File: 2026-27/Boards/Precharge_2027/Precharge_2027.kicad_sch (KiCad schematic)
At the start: 88 parts, among them J1 0430450812, J2 Conn_01x04_Pin, J3 Conn_01x02_Pin, Q1 XR6005, Q2 XR6005, Q3 AO3407, Q5 AO3407, U1 H11L1, U2 LM331N, U4 H11L1, U5 LM331N, U7 STM32C011F6P6, U8 UA78M33QDCYRQ1, X1 X50328MSB2GI

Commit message: Update Precharge 2027
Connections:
- net at Molex1.1 (Pin_1): now also F2.2, Molex1.2 (Pin_2)
- net at Molex3.1 (Pin_1): now also F3.2, Molex3.2 (Pin_2)
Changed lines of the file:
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@@
+	)
+	(junction
+		(at 22.86 52.07)
+		(diameter 0)
+		(color 0 0 0 0)
 	)
 	(junction
@@
 	)
 	(junction
+		(at 22.86 181.61)
+		(diameter 0)
+		(color 0 0 0 0)
+	)
+	(junction
 		(at 173.99 41.91)
 		(diameter 0)
@@
 	)
 	(junction
-		(at 22.86 181.61)
-		(diameter 0)
-		(color 0 0 0 0)
-	)
-	(junction
 		(at 266.7 124.46)
 		(diameter 0)
@@
 	)
 	(junction
+		(at 22.86 108.585)
+		(diameter 0)
+		(color 0 0 0 0)
+	)
+	(junction
 		(at 135.255 65.405)
 		(diameter 0)
@@
 	)
 	(junction
+		(at 22.86 128.27)
+		(diameter 0)
+		(color 0 0 0 0)
+	)
+	(junction
 		(at 300.99 114.3)
 		(diameter 0)
@@
 	(junction
 		(at 115.57 68.58)
-		(diameter 0)
-		(color 0 0 0 0)
-	)
-	(junction
-		(at 22.86 107.95)
 		(diameter 0)
 		(color 0 0 0 0)
@@
 	(wire
 		(pts
-			(xy 22.86 107.95) (xy 22.86 110.49)
+			(xy 22.86 107.95) (xy 22.86 108.585)
 		)
 		(stroke
@@
 	(wire
 		(pts
+			(xy 22.86 108.585) (xy 50.165 108.585)
+		)
+		(stroke
+			(width 0)
+			(type default)
+		)
+	)
+	(wire
+		(pts
 			(xy 307.975 73.025) (xy 307.975 77.47)
 		)
@@
 	(wire
 		(pts
-			(xy 22.86 107.95) (xy 50.8 107.95)
-		)
-		(stroke
-			(width 0)
-			(type default)
-		)
-	)
-	(wire
-		(pts
 			(xy 132.08 109.22) (xy 132.08 113.03)
 		)
@@
 	(wire
 		(pts
+			(xy 22.86 52.07) (xy 22.86 54.61)
+		)
+		(stroke
+			(width 0)
+			(type default)
+		)
+	)
+	(wire
+		(pts
 			(xy 335.28 181.61) (xy 339.09 181.61)
 		)
@@
 	(wire
 		(pts
+			(xy 50.165 108.585) (xy 50.8 107.95)
+		)
+		(stroke
+			(width 0)
+			(type default)
+		)
+	)
+	(wire
+		(pts
 			(xy 71.12 146.05) (xy 80.01 146.05)
 		)
@@
 	(wire
 		(pts
+			(xy 22.86 108.585) (xy 22.86 110.49)
+		)
+		(stroke
+			(width 0)
+			(type default)
+		)
+	)
+	(wire
+		(pts
 			(xy 133.35 186.69) (xy 134.62 186.69)
 		)
@@
 	(wire
 		(pts
+			(xy 76.2 96.52) (xy 78.74 96.52)
+		)
+		(stroke
+			(width 0)
+			(type default)
+		)
+	)
+	(wire
+		(pts
+			(xy 170.18 154.94) (xy 161.29 154.94)
+		)
+		(stroke
+			(width 0)
+			(type default)
+		)
+	)
+	(wire
+		(pts
+			(xy 22.86 128.27) (xy 22.86 130.81)
+		)
+		(stroke
+			(width 0)
+			(type default)
+		)
+	)
+	(wire
+		(pts
+			(xy 220.98 29.21) (xy 218.44 29.21)
+		)
+		(stroke
+			(width 0)
+			(type default)
+		)
+	)
+	(wire
+		(pts
+			(xy 310.515 73.025) (xy 310.515 77.47)
+		)
+		(stroke
+			(width 0)
+			(type default)
+		)
+	)
+	(wire
+		(pts
+			(xy 50.8 93.98) (xy 54.61 93.98)
+		)
+		(stroke
+			(width 0)
+			(type default)
+		)
+	)
+	(wire
+		(pts
 			(xy 22.86 181.61) (xy 46.99 181.61)
 		)
 		(stroke
-			(width 0)
-			(type default)
-		)
-	)
-	(wire
-		(pts
-			(xy 76.2 96.52) (xy 78.74 96.52)
-		)
-		(stroke
-			(width 0)
-			(type default)
-		)
-	)
-	(wire
-		(pts
-			(xy 170.18 154.94) (xy 161.29 154.94)
-		)
-		(stroke
-			(width 0)
-			(type default)
-		)
-	)
-	(wire
-		(pts
-			(xy 220.98 29.21) (xy 218.44 29.21)
-		)
-		(stroke
-			(width 0)
-			(type default)
-		)
-	)
-	(wire
-		(pts
-			(xy 310.515 73.025) (xy 310.515 77.47)
-		)
-		(stroke
-			(width 0)
-			(type default)
-		)
-	)
-	(wire
-		(pts
-			(xy 50.8 93.98) (xy 54.61 93.98)
-		)
-		(stroke

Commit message: Precharge 2027 Changes, outlined in Discord, Systems-Electric
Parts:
- removed C1: 22uF, easyeda2kicad:C0805, symbol easyeda2kicad:CL21A226MAQNNNE
- removed D3: PESD15VS1UB, Diode_SMD:D_SOD-523, symbol Diode:PESD3V3S1UL
- removed PS1: TBA_1-1212E, footprints:CONV_TBA_1-1212E, symbol TBA_1-1212E:TBA_1-1212E
- removed TP1, TP2: TestPoint, TestPoint:TestPoint_Pad_D3.0mm, symbol Connector:TestPoint
- removed U8: UA78M33QDCYRQ1, easyeda2kicad:SOT-223-3_L6.5-W3.4-P2.30-LS7.0-BR, symbol easyeda2kicad:UA78M33QDCYRG4Q1
- added C1: C2012X5R1V226MT000E, easyeda2kicad:C0805, symbol easyeda2kicad:C2012X5R1V226MT000E
- added D1: SMAJ30CA_C10755, easyeda2kicad:SMA_L4.4-W2.6-LS5.0-BI, symbol easyeda2kicad:SMAJ30CA_C10755
- added PS1: IM2412SA, IM2405S, symbol easyeda2kicad:IM2412SA
- added U3: MIC5239-3.3YS, easyeda2kicad:SOT-223-3_L6.7-W3.7-P2.30-LS7.0-BR, symbol easyeda2kicad:MIC5239-3.3YS
- D4, D5: value MMBZ16VALT1G -> MMBZ33VALT1G; symbol easyeda2kicad:MMBZ16VALT1G -> easyeda2kicad:MMBZ33VALT1G; LCSC Part C891696 -> C185935; MPN MMBZ16VALT1G -> MMBZ33VALT1G
- Q3, Q5: value AO3407 -> DMP510DL-7; symbol easyeda2kicad:AO3407 -> easyeda2kicad:DMP510DL-7; LCSC Part C181093 -> C397953; MPN AO3407 -> DMP510DL-7; Manufacturer Hottech(合科泰) -> DIODES(美台)
- R18, R30: footprint easyeda2kicad:R0603 -> easyeda2kicad:R0805; symbol easyeda2kicad:0603WAJ0103T5E -> easyeda2kicad:0805W8F1002T5E; LCSC Part C15401 -> C17414; MPN (none) -> 0805W8F1002T5E; Manufacturer (none) -> UNI-ROYAL(厚声)
- R19, R29: footprint easyeda2kicad:R0603 -> easyeda2kicad:R0805; symbol easyeda2kicad:0603WAF3302T5E -> easyeda2kicad:0805W8F3302T5E; LCSC Part C4216 -> C17633; MPN (none) -> 0805W8F3302T5E; Manufacturer (none) -> UNI-ROYAL(厚声)
- ZD6: renamed from D6; value BZT52C10S -> BZT52C24_C2109; footprint Diode_SMD:D_SOD-323 -> easyeda2kicad:SOD-123_L2.8-W1.8-LS3.7-RD; symbol PCM_JLCPCB-Diodes:Zener,BZT52C10S -> easyeda2kicad:BZT52C24_C2109; Attrition Qty 6 -> (none); Category Diodes,Zener Diodes -> (none); Class Preferred Component -> (none); LCSC C19077446 -> (none); LCSC Part (none) -> C2109; MPN (none) -> BZT52C24; Manufacturer hongjiacheng -> CJ(江苏长电/长晶); Minimum Qty 20 -> (none); Part BZT52C10S -> (none); Price 0.019USD -> (none); Process SMT -> (none); Stock 178615 -> (none)
- renumbered F3 to F1
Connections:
- net 12V_HV: now also D1.2 (A), PS1.6 (+V_OUTPUT)
- net 3.3 V: now also C14.2, U3.3 (OUT); no longer C14.1
- net GLV+: now also C1.2, PS1.2 (+V_INPUT), U3.1 (IN)
- net GLV-: now also C14.1, C1.1, PS1.1 (-V_INPUT), PS1.3 (REMOTE_ON/OFF), U3.2 (GND), U3.4 (GND); no longer C14.2
- net HV-: now also D1.1 (K), PS1.9 (-V_OUTPUT)
- no-connect marks 6 -> 8
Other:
- note added: "3.3V LDO Source"
- note added: "33V ESD/Surge TVS Zener Diodes"
- note added: "Active Low Signals"
- note added: "Charge Mode"
- note added: "Charge_on is tied to GND in the charge cart, and floating (pulled high)when not connected to the charge cart so CHG is ON or OFF respectively"
- note added: "Isolated 12V source"
- note added: "MCU"
- note added: "Post AIR Voltage to Frequency Converter"
- note added: "Pre AIR Voltage to Frequency Converter"
- note removed: "Charge_on is tied to GND in the charge cart, and floating (pulled high) when not connected to the charge cart so CHG is ON or OFF respectively"
- note removed: "Isolated 12V source LV side HV side"
- note removed: "active low signals"
- moved on the sheet: C10, C11, C14, C15, C16, C17, C2, C3, C4, C5, C6, C7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

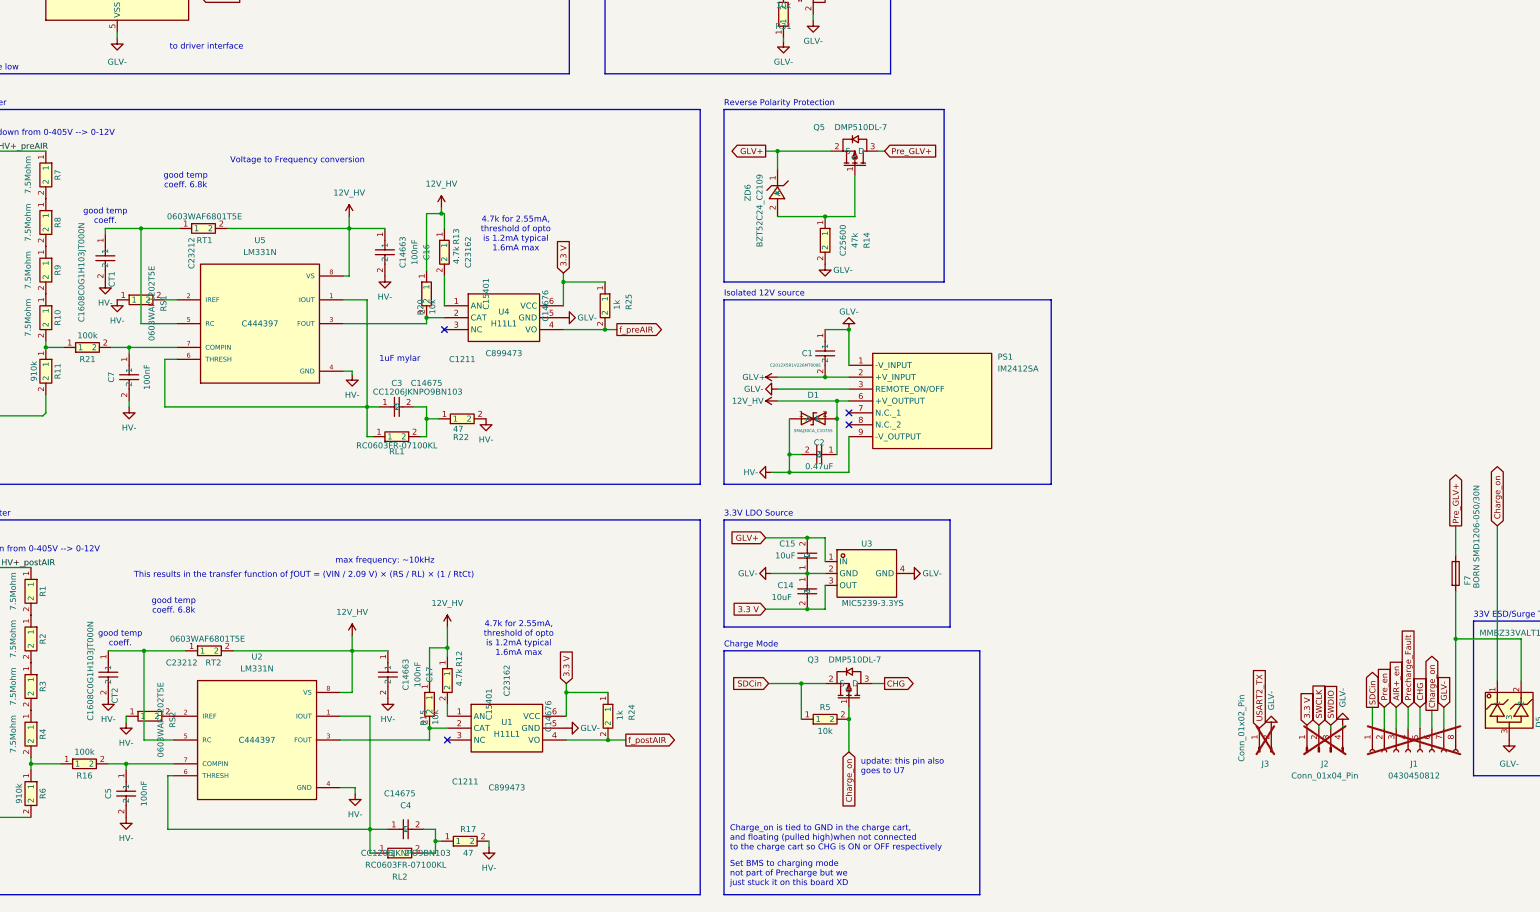
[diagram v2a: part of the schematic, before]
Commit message: precharge 2027 isolation fixing, passing it to Nick for layout
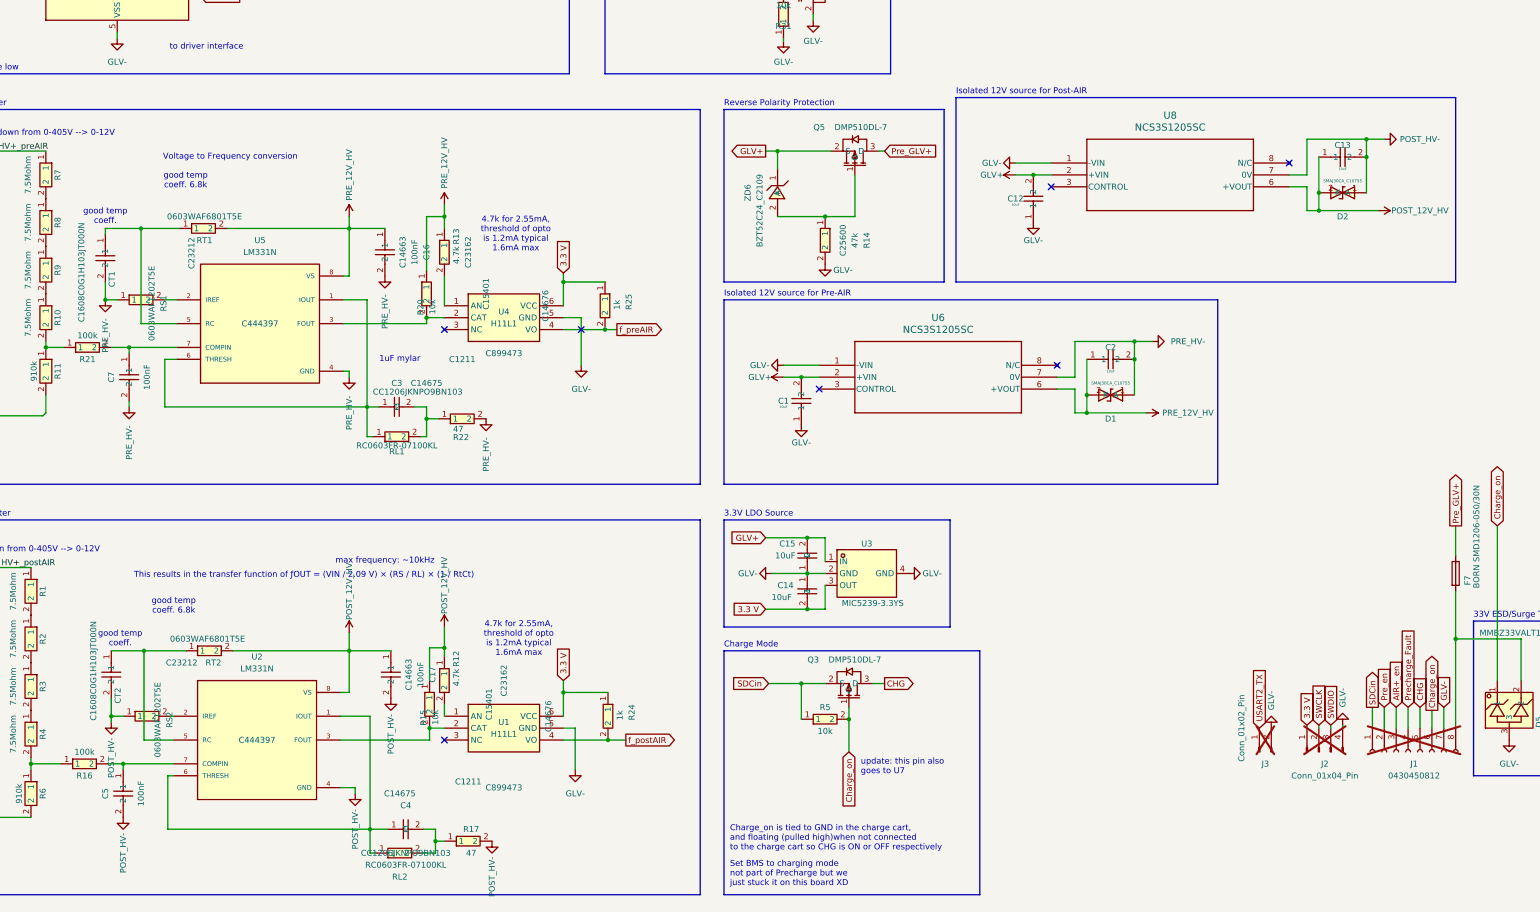
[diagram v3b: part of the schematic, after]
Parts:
- removed PS1: IM2412SA, IM2405S, symbol easyeda2kicad:IM2412SA
- added C12, C13: 10uF, easyeda2kicad:C0805, symbol easyeda2kicad:GRM21BR61H106KE43L
- added D2: SMAJ30CA_C10755, easyeda2kicad:SMA_L4.4-W2.6-LS5.0-BI, symbol easyeda2kicad:SMAJ30CA_C10755
- added U6, U8: NCS3S1205SC, easyeda2kicad:NCS3S1205SC_MUR, symbol easyeda2kicad:NCS3S1205SC
- C1: value C2012X5R1V226MT000E -> 10uF; symbol easyeda2kicad:C2012X5R1V226MT000E -> easyeda2kicad:GRM21BR61H106KE43L; LCSC Part C338080 -> C440198; MPN C2012X5R1V226MT000E -> GRM21BR61H106KE43L; Manufacturer TDK -> muRata(村田)
- C2: value 0.47uF -> 10uF; symbol easyeda2kicad:CL21B474KBFNNNE -> easyeda2kicad:GRM21BR61H106KE43L; LCSC Part C13967 -> C440198; MPN (none) -> GRM21BR61H106KE43L; Manufacturer (none) -> muRata(村田)
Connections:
- net GLV+: now also C12.2, U6.2 (+VIN), U8.2 (+VIN)
- net GLV-: now also C12.1, U6.1 (-VIN), U8.1 (-VIN)
- net 12V_HV renamed PRE_12V_HV
- net PRE_12V_HV: now also U6.6 (+VOUT); no longer C17.1, R12.1, R15.1, RT2.2, U2.8 (VS)
- net HV- renamed PRE_HV-
- net PRE_HV-: now also U6.7 (0V); no longer C17.2, C5.2, CT2.2, R17.2, RS2.1, U2.4 (GND)
- new net POST_12V_HV: C13.1, C17.1, D2.2 (A), R12.1, R15.1, RT2.2, U2.8 (VS), U8.6 (+VOUT)
- new net POST_HV-: C13.2, C17.2, C5.2, CT2.2, D2.1 (K), R17.2, RS2.1, U2.4 (GND), U8.7 (0V)
- no-connect marks 8 -> 11
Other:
- note added: "Isolated 12V source for Post-AIR"
- note added: "Isolated 12V source for Pre-AIR"
- note removed: "Isolated 12V source"
- moved on the sheet: C1, C17, C2, C5, CT2, D1, R12, R17, RS2, U1

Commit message: Update Precharge 2027 design
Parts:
- C3, C4: value CC1206JKNPO9BN103 -> 100nF C0G; symbol easyeda2kicad:CC1206JKNPO9BN103 -> easyeda2kicad:CC1206JKNPO9BN104; LCSC Part C326648 -> C577121; MPN CC1206JKNPO9BN103 -> CC1206JKNPO9BN104; Manufacturer YAGEO(国巨) -> YAGEO
- R1, R10, R2, R3, R4, R7, R8, R9: value 7.5Mohm -> 1.00M; symbol easyeda2kicad:FRC1206F7504TS -> easyeda2kicad:RT1206BRD071ML; LCSC Part C2999556 -> C309662; MPN FRC1206F7504TS -> RT1206BRD071ML; Manufacturer FOJAN(富捷) -> YAGEO
- R11, R6: value 910k -> 80.6k; symbol easyeda2kicad:FRC0603F9103TS -> easyeda2kicad:RT0603BRD0780K6L; LCSC Part C2907075 -> C861568; MPN FRC0603F9103TS -> RT0603BRD0780K6L; Manufacturer FOJAN(富捷) -> YAGEO
- R16, R21: value 100k -> 21.0k; symbol easyeda2kicad:0603WAJ0104T5E -> easyeda2kicad:RT0603BRD0721KL; LCSC Part C15458 -> C861228; MPN (none) -> RT0603BRD0721KL; Manufacturer (none) -> YAGEO
- RL1, RL2: value RC0603FR-07100KL -> 100k; symbol easyeda2kicad:RC0603FR-07100KL -> easyeda2kicad:RT0603BRD07100KL; LCSC Part C14675 -> C122538; MPN (none) -> RT0603BRD07100KL; Manufacturer (none) -> YAGEO
- RS1, RS2: value 0603WAF1202T5E -> 17.8k; symbol easyeda2kicad:0603WAF1202T5E -> easyeda2kicad:RT0603BRD0717K8L; LCSC Part C22790 -> C705729; MPN (none) -> RT0603BRD0717K8L; Manufacturer (none) -> YAGEO

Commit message: moving accumulator boards: ETS and celltap pos/neg boards to github
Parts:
- U6, U8: now not fitted; now left out of the parts list
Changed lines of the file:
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@@
 		(body_style 1)
 		(exclude_from_sim no)
-		(in_bom yes)
+		(in_bom no)
 		(on_board yes)
 		(in_pos_files yes)
-		(dnp no)
+		(dnp yes)
 		(property "Reference" "U6"
 			(at 254 151.13 0)
@@
 		(body_style 1)
 		(exclude_from_sim no)
-		(in_bom yes)
+		(in_bom no)
 		(on_board yes)
 		(in_pos_files yes)
-		(dnp no)
+		(dnp yes)
 		(property "Reference" "U8"
 			(at 303.53 107.95 0)
